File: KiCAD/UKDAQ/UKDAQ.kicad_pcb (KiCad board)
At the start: 2 copper layers, 22 parts, among them J1 5 pin Molex (0537800570), U1 AP2210N_SOT-23-3, U2 PI4ULS5V202, U3 BNO055, U4 BME280, U5 MAX32660-24TQFN-EP, Y1 Crystal

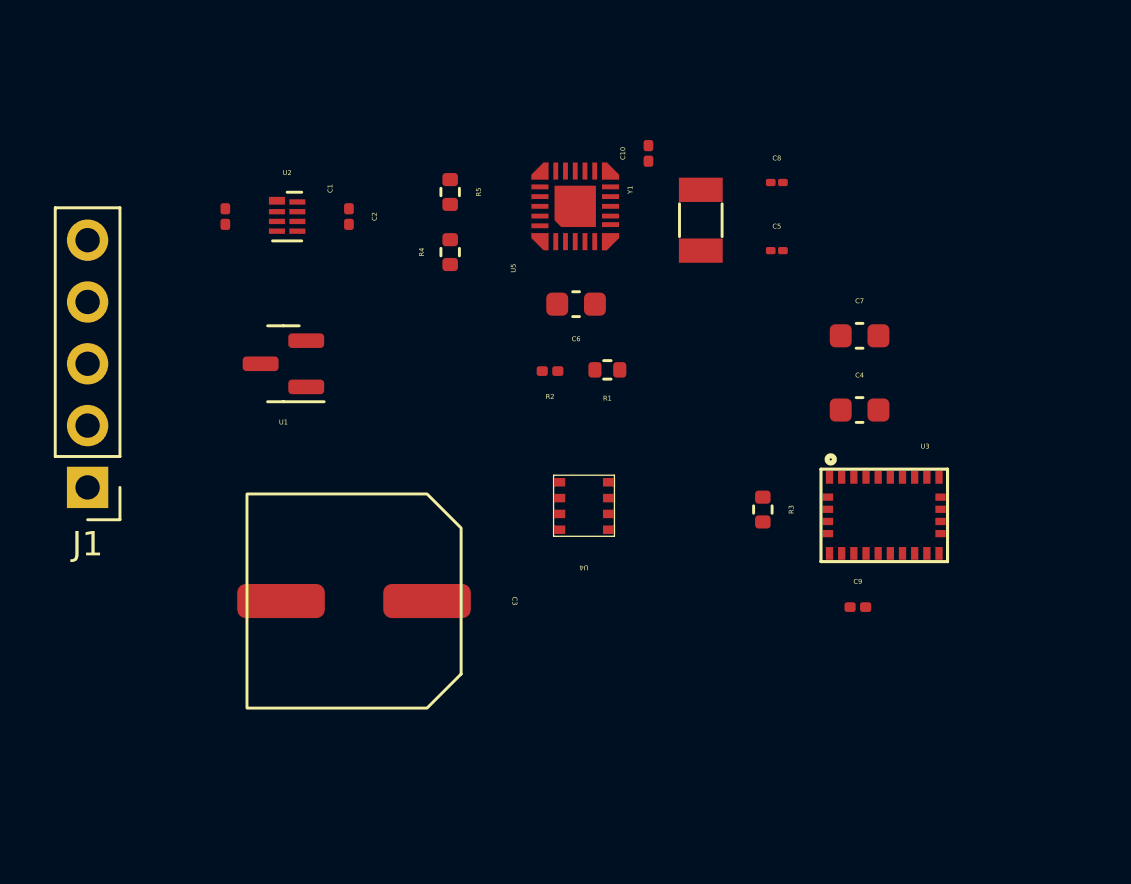
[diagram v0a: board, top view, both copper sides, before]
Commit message: routed traces (LAZY AS FUCK) gonna do ground pour and ground pads tommorow
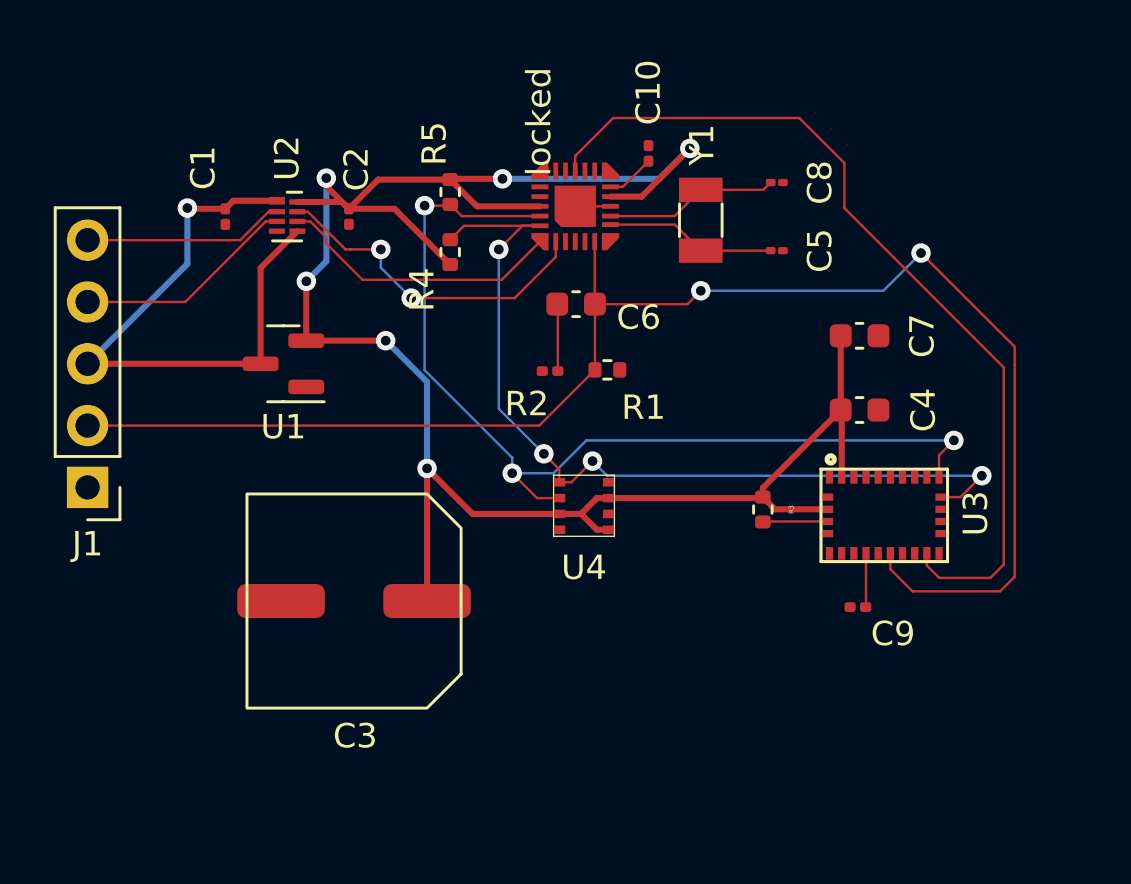
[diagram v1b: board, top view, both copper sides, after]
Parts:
- renumbered U5 to locked
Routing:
- net VDD: track 0.00 -> 83.8 mm, vias 0 -> 6
- net /nRESET: track 0.00 -> 62.6 mm, vias 0 -> 2
- net /SDA: track 0.00 -> 40.3 mm, vias 0 -> 3
- net /SCL: track 0.00 -> 36.7 mm, vias 0 -> 4
- net /BNO_INTERRUPT: track 0.00 -> 36.4 mm
- net VCC: track 0.00 -> 25.1 mm, vias 0 -> 1
- net /TX/SWDIO-VDD: track 0.00 -> 13.9 mm, vias 0 -> 2
- net /RX/SWCLK-VDD: track 0.00 -> 11.8 mm
- net /RX/SWCLK-VCC: track 0.00 -> 9.15 mm
- net /TX/SWDIO-VCC: track 0.00 -> 8.26 mm
- net Net-(C8-Pad1): track 0.00 -> 7.16 mm
- net Net-(C5-Pad1): track 0.00 -> 7.03 mm
- net Net-(C6-Pad2): track 0.00 -> 2.76 mm
- net Net-(R3-Pad2): track 0.00 -> 2.69 mm
- net Net-(C9-Pad2): track 0.00 -> 2.21 mm
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
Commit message: PCB done yippe probably gonna haftaredo la8r
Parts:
- removed locked: MAX32660-24TQFN-EP, Joseph:MAX32660-24-TQFN-EP
- added U5: MAX32660-24TQFN-EP, Joseph:MAX32660-24-TQFN-EP, F.Cu at (146.3, 102.4)
- moved C8 16.7 mm to (147.2, 109.4), turned to 180 degrees
- moved C5 14.6 mm to (145.3, 109.4)
- moved C10 14.1 mm to (149.0, 105.4), turned to 0 degrees
- moved C9 13.6 mm to (155.0, 96.9), turned to -90 degrees
- moved Y1 12.9 mm to (146.2, 107.4), turned to 0 degrees
- moved C7 12.2 mm to (156.9, 111.1)
- moved U4 11.4 mm to (152.8, 111.4)
- moved R5 11.4 mm to (146.8, 99.3), turned to 180 degrees
- moved R3 11.2 mm to (159.3, 100.2), turned to 90 degrees
- moved R4 8.26 mm to (144.6, 99.3), turned to 0 degrees
- moved J1 6.64 mm to (123.6, 99.0), turned to 0 degrees
- moved U3 6.40 mm to (154.2, 100.3), turned to 180 degrees
- moved R2 6.23 mm to (143.0, 106.7), turned to -90 degrees
- moved C6 6.04 mm to (143.0, 104.0), turned to -90 degrees
- moved C2 5.94 mm to (136.5, 99.1), turned to 0 degrees
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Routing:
- net /BNO_INTERRUPT: track 36.4 -> 8.56 mm
- net /nRESET: track 62.6 -> 41.9 mm
- net /SDA: track 40.3 -> 19.7 mm, vias 3 -> 2
- net /SCL: track 36.7 -> 20.4 mm, vias 4 -> 2
- net /TX/SWDIO-VCC: track 8.26 -> 16.9 mm, vias 0 -> 1
- net GND: track 1.45 -> 8.55 mm, vias 0 -> 16
- net VDD: track 83.8 -> 87.7 mm, vias 6 -> 3
- net /RX/SWCLK-VCC: track 9.15 -> 12.3 mm, vias 0 -> 1
- net VCC: track 25.1 -> 27.2 mm, vias 1 -> 0
- net Net-(C5-Pad1): track 7.03 -> 5.79 mm
- net /TX/SWDIO-VDD: track 13.9 -> 12.6 mm
- net Net-(C6-Pad2): track 2.76 -> 1.63 mm
- net Net-(C8-Pad1): track 7.16 -> 6.21 mm
- net Net-(C10-Pad1): track 2.00 -> 2.76 mm
- net Net-(C9-Pad2): track 2.21 -> 1.58 mm
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- added copper zone on B.Cu, net GND
- added copper zone on F.Cu, net GND
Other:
- board outline added: 41 x 24.5 mm
- rule pad_to_mask_clearance: 0 -> 0.0508
